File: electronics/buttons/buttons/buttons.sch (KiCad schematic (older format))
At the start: 12 parts, among them J1 Conn_01x02_Male, J2 Conn_01x03_Male, J3 Conn_01x03_Male

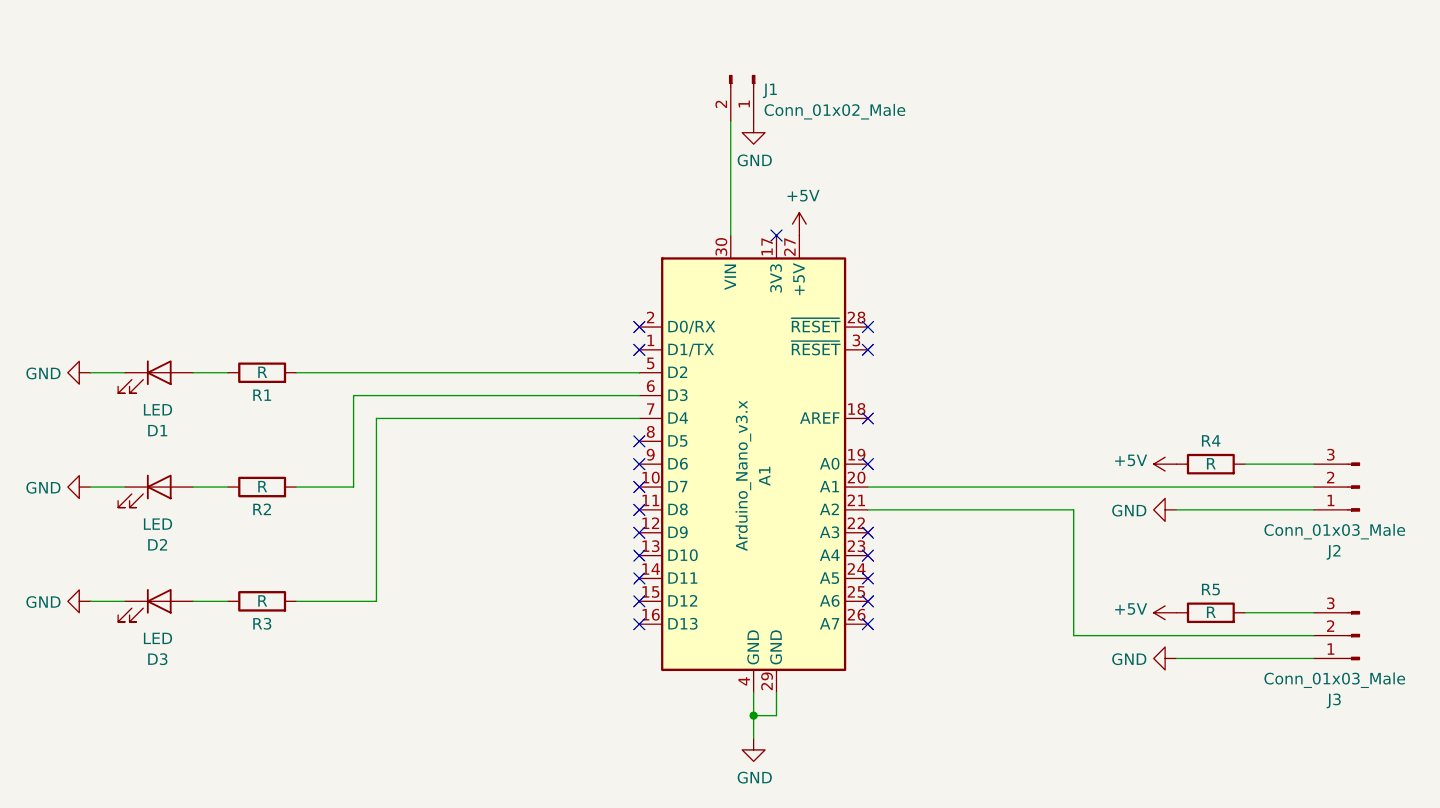
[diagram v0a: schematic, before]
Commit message: change button pcb layout. Added fab files
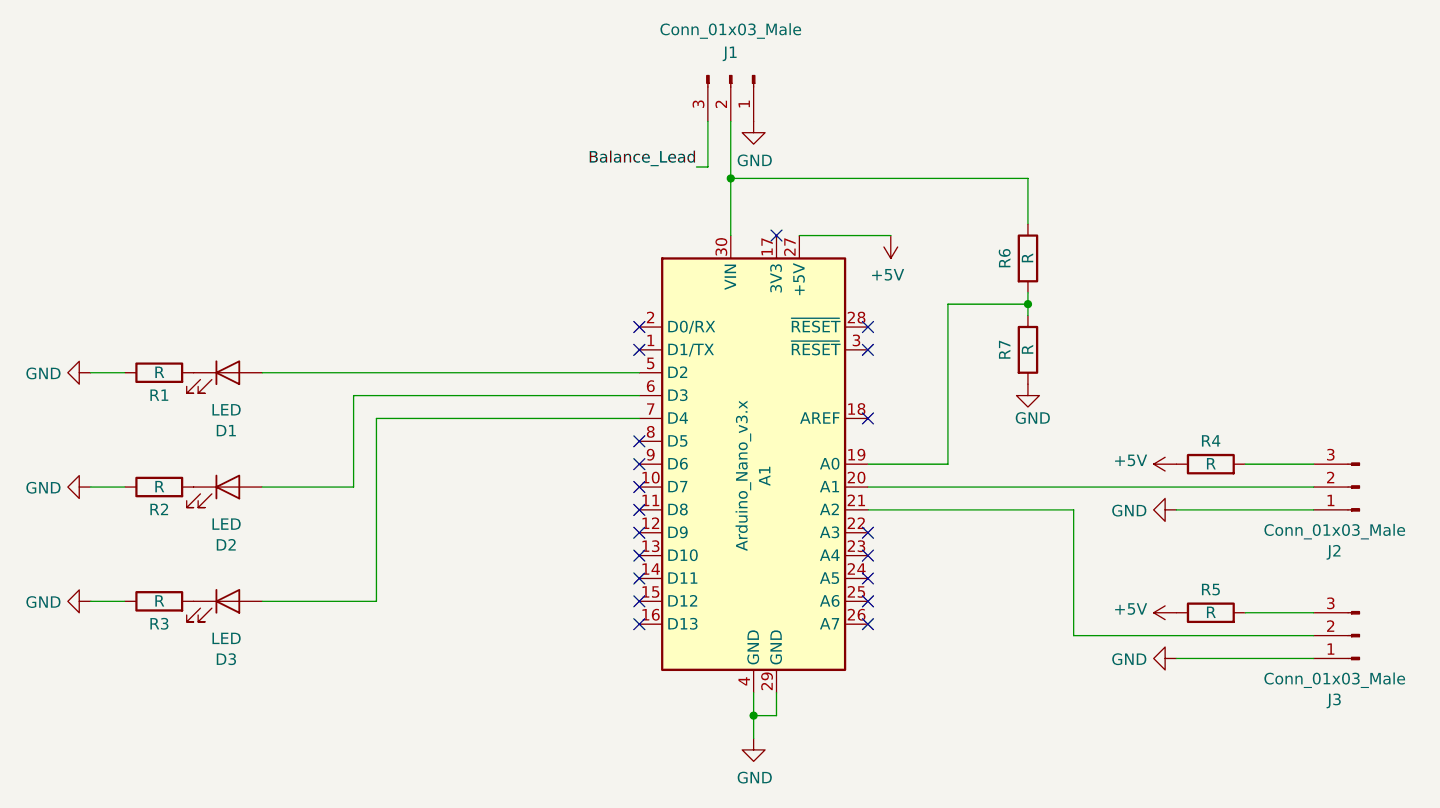
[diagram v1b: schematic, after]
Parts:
- removed J1: Conn_01x02_Male, Connector_JST:JST_EH_S2B-EH_1x02_P2.50mm_Horizontal, symbol Connector:Conn_01x02_Male
- added J1: Conn_01x03_Male, Connector_PinHeader_2.54mm:PinHeader_1x03_P2.54mm_Vertical, symbol Connector:Conn_01x03_Male
- added R6, R7: R, Resistor_SMD:R_1206_3216Metric_Pad1.42x1.75mm_HandSolder, symbol Device:R
- A1: footprint Module:Arduino_Nano -> 1_Project_Specific:NANO_33_Footprint_SMD_Castell
- J2, J3: footprint Connector_JST:JST_XH_B3B-XH-A_1x03_P2.50mm_Vertical -> Connector_PinHeader_2.54mm:PinHeader_1x03_P2.54mm_Vertical
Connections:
- net GND: now also R1.1, R2.1, R3.1, J1.1 (Pin_1), R7.2; no longer D1.1 (K), D2.1 (K), D3.1 (K)
- net at A1.19 (A0): now also R6.2, R7.1
- net at A1.30 (VIN): now also J1.2 (Pin_2), R6.1
- net at A1.5 (D2): now also D1.2 (A); no longer R1.2
- net at A1.6 (D3): now also D2.2 (A); no longer R2.2
- net at A1.7 (D4): now also D3.2 (A); no longer R3.2
- new net: D3.1 (K), R3.2
- new net: D2.1 (K), R2.2
- new net: D1.1 (K), R1.2
- new net Balance_Lead: J1.3 (Pin_3)
- no-connect marks 21 -> 20
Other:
- moved on the sheet: D1, D2, D3, R1, R2, R3
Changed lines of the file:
@@
 F 0 "A1" V 4800 3300 50  0000 C CNN
 F 1 "Arduino_Nano_v3.x" V 4700 3300 50  0000 C CNN
-F 2 "Module:Arduino_Nano" H 4750 3350 50  0001 C CIN
+F 2 "1_Project_Specific:NANO_33_Footprint_SMD_Castell" H 4750 3350 50  0001 C CIN
 F 3 "http://www.mouser.com/pdfdocs/Gravitech_Arduino_Nano3_0.pdf" H 4750 3350 50  0001 C CNN
 	1    4750 3350
@@
 L Device:LED D3
 U 1 1 5E72B9A4
+P 2450 3950
+F 0 "D3" H 2443 3695 50  0000 C CNN
+F 1 "LED" H 2443 3786 50  0000 C CNN
+F 2 "LED_THT:LED_D5.0mm" H 2450 3950 50  0001 C CNN
+F 3 "~" H 2450 3950 50  0001 C CNN
+	1    2450 3950
+	1    0    0    -1
+$EndComp
+$Comp
+L Device:LED D2
+U 1 1 5E72CADD
+P 2450 3450
+F 0 "D2" H 2443 3195 50  0000 C CNN
+F 1 "LED" H 2443 3286 50  0000 C CNN
+F 2 "LED_THT:LED_D5.0mm" H 2450 3450 50  0001 C CNN
+F 3 "~" H 2450 3450 50  0001 C CNN
+	1    2450 3450
+	1    0    0    -1
+$EndComp
+$Comp
+L Device:LED D1
+U 1 1 5E72CFE8
+P 2450 2950
+F 0 "D1" H 2443 2695 50  0000 C CNN
+F 1 "LED" H 2443 2786 50  0000 C CNN
+F 2 "LED_THT:LED_D5.0mm" H 2450 2950 50  0001 C CNN
+F 3 "~" H 2450 2950 50  0001 C CNN
+	1    2450 2950
+	1    0    0    -1
+$EndComp
+$Comp
+L Device:R R3
+U 1 1 5E72D9E9
 P 2150 3950
-F 0 "D3" H 2143 3695 50  0000 C CNN
-F 1 "LED" H 2143 3786 50  0000 C CNN
-F 2 "LED_THT:LED_D5.0mm" H 2150 3950 50  0001 C CNN
+F 0 "R3" V 2050 3950 50  0000 C CNN
+F 1 "R" V 2150 3950 50  0000 C CNN
+F 2 "Resistor_SMD:R_1206_3216Metric_Pad1.42x1.75mm_HandSolder" V 2080 3950 50  0001 C CNN
 F 3 "~" H 2150 3950 50  0001 C CNN
 	1    2150 3950
-	1    0    0    -1
-$EndComp
-$Comp
-L Device:LED D2
-U 1 1 5E72CADD
+	0    -1   -1   0
+$EndComp
+$Comp
+L Device:R R2
+U 1 1 5E72E3E8
 P 2150 3450
-F 0 "D2" H 2143 3195 50  0000 C CNN
-F 1 "LED" H 2143 3286 50  0000 C CNN
-F 2 "LED_THT:LED_D5.0mm" H 2150 3450 50  0001 C CNN
+F 0 "R2" V 2050 3450 50  0000 C CNN
+F 1 "R" V 2150 3450 50  0000 C CNN
+F 2 "Resistor_SMD:R_1206_3216Metric_Pad1.42x1.75mm_HandSolder" V 2080 3450 50  0001 C CNN
 F 3 "~" H 2150 3450 50  0001 C CNN
 	1    2150 3450
-	1    0    0    -1
-$EndComp
-$Comp
-L Device:LED D1
-U 1 1 5E72CFE8
+	0    -1   -1   0
+$EndComp
+$Comp
+L Device:R R1
+U 1 1 5E72E9E3
 P 2150 2950
-F 0 "D1" H 2143 2695 50  0000 C CNN
-F 1 "LED" H 2143 2786 50  0000 C CNN
-F 2 "LED_THT:LED_D5.0mm" H 2150 2950 50  0001 C CNN
+F 0 "R1" V 2050 2950 50  0000 C CNN
+F 1 "R" V 2150 2950 50  0000 C CNN
+F 2 "Resistor_SMD:R_1206_3216Metric_Pad1.42x1.75mm_HandSolder" V 2080 2950 50  0001 C CNN
 F 3 "~" H 2150 2950 50  0001 C CNN
 	1    2150 2950
-	1    0    0    -1
-$EndComp
-$Comp
-L Device:R R3
-U 1 1 5E72D9E9
-P 2600 3950
-F 0 "R3" V 2500 3950 50  0000 C CNN
-F 1 "R" V 2600 3950 50  0000 C CNN
-F 2 "Resistor_SMD:R_1206_3216Metric_Pad1.42x1.75mm_HandSolder" V 2530 3950 50  0001 C CNN
-F 3 "~" H 2600 3950 50  0001 C CNN
-	1    2600 3950
-	0    -1   -1   0
-$EndComp
-$Comp
-L Device:R R2
-U 1 1 5E72E3E8
-P 2600 3450
-F 0 "R2" V 2500 3450 50  0000 C CNN
-F 1 "R" V 2600 3450 50  0000 C CNN
-F 2 "Resistor_SMD:R_1206_3216Metric_Pad1.42x1.75mm_HandSolder" V 2530 3450 50  0001 C CNN
-F 3 "~" H 2600 3450 50  0001 C CNN
-	1    2600 3450
-	0    -1   -1   0
-$EndComp
-$Comp
-L Device:R R1
-U 1 1 5E72E9E3
-P 2600 2950
-F 0 "R1" V 2500 2950 50  0000 C CNN
-F 1 "R" V 2600 2950 50  0000 C CNN
-F 2 "Resistor_SMD:R_1206_3216Metric_Pad1.42x1.75mm_HandSolder" V 2530 2950 50  0001 C CNN
-F 3 "~" H 2600 2950 50  0001 C CNN
-	1    2600 2950
 	0    -1   -1   0
 $EndComp
@@
 F 0 "J2" H 7508 3731 50  0000 C CNN
 F 1 "Conn_01x03_Male" H 7508 3640 50  0000 C CNN
-F 2 "Connector_JST:JST_XH_B3B-XH-A_1x03_P2.50mm_Vertical" H 7400 3450 50  0001 C CNN
+F 2 "Connector_PinHeader_2.54mm:PinHeader_1x03_P2.54mm_Vertical" H 7400 3450 50  0001 C CNN
 F 3 "~" H 7400 3450 50  0001 C CNN
 	1    7400 3450
@@
 F 0 "J3" H 7508 4381 50  0000 C CNN
 F 1 "Conn_01x03_Male" H 7508 4290 50  0000 C CNN
-F 2 "Connector_JST:JST_XH_B3B-XH-A_1x03_P2.50mm_Vertical" H 7400 4100 50  0001 C CNN
+F 2 "Connector_PinHeader_2.54mm:PinHeader_1x03_P2.54mm_Vertical" H 7400 4100 50  0001 C CNN
 F 3 "~" H 7400 4100 50  0001 C CNN
 	1    7400 4100
 	-1   0    0    1
 $EndComp
-Wire Wire Line
-	2450 3450 2300 3450
-Wire Wire Line
-	2450 3950 2300 3950
-Wire Wire Line
-	2450 2950 2300 2950
 Wire Wire Line
 	6900 3350 7200 3350
@@
 	3000 3050 3000 3450
 Wire Wire Line
-	3000 3450 2750 3450
-Wire Wire Line
 	3100 3150 3100 3950
-Wire Wire Line
-	3100 3950 2750 3950
-Wire Wire Line
-	2750 2950 4250 2950
 Wire Wire Line
 	3000 3050 4250 3050
@@
 	1    0    0    -1
 $EndComp
-$Comp
-L Connector:Conn_01x02_Male J1
-U 1 1 5E762A53
-P 4750 1650
-F 0 "J1" V 4812 1694 50  0000 L CNN
-F 1 "Conn_01x02_Male" V 4903 1694 50  0000 L CNN
-F 2 "Connector_JST:JST_EH_S2B-EH_1x02_P2.50mm_Horizontal" H 4750 1650 50  0001 C CNN
-F 3 "~" H 4750 1650 50  0001 C CNN
-	1    4750 1650
-	0    1    1    0
-$EndComp
-Wire Wire Line
-	4650 2350 4650 1850
-$Comp
-L power:GND #PWR0109
-U 1 1 5E764900
-P 4750 1850
-F 0 "#PWR0109" H 4750 1600 50  0001 C CNN
-F 1 "GND" H 4755 1677 50  0000 C CNN
-F 2 "" H 4750 1850 50  0001 C CNN
-F 3 "" H 4750 1850 50  0001 C CNN
-	1    4750 1850
-	1    0    0    -1
-$EndComp
+Wire Wire Line
+	4650 2350 4650 2100
 $Comp
 L power:+5V #PWR0110
 U 1 1 5E7657A9
-P 4950 2350
-F 0 "#PWR0110" H 4950 2200 50  0001 C CNN
-F 1 "+5V" H 4965 2523 50  0000 C CNN
-F 2 "" H 4950 2350 50  0001 C CNN
-F 3 "" H 4950 2350 50  0001 C CNN
-	1    4950 2350
-	1    0    0    -1
+P 5350 2350
+F 0 "#PWR0110" H 5350 2200 50  0001 C CNN
+F 1 "+5V" H 5365 2523 50  0000 C CNN
+F 2 "" H 5350 2350 50  0001 C CNN
+F 3 "" H 5350 2350 50  0001 C CNN
+	1    5350 2350
+	-1   0    0    1
 $EndComp
 NoConn ~ 4850 2350
@@
 NoConn ~ 5250 3750
 NoConn ~ 5250 3650
-NoConn ~ 5250 3350
+$Comp
+L Connector:Conn_01x03_Male J1
+U 1 1 5E737BF0
+P 4650 1650
+F 0 "J1" V 4550 1650 50  0000 C CNN
+F 1 "Conn_01x03_Male" V 4450 1650 50  0000 C CNN
+F 2 "Connector_PinHeader_2.54mm:PinHeader_1x03_P2.54mm_Vertical" H 4650 1650 50  0001 C CNN
+F 3 "~" H 4650 1650 50  0001 C CNN
+	1    4650 1650
+	0    1    1    0
+$EndComp
+$Comp
+L power:GND #PWR0109
+U 1 1 5E764900
+P 4750 1850
+F 0 "#PWR0109" H 4750 1600 50  0001 C CNN
+F 1 "GND" H 4755 1677 50  0000 C CNN
+F 2 "" H 4750 1850 50  0001 C CNN
+F 3 "" H 4750 1850 50  0001 C CNN
+	1    4750 1850
+	1    0    0    -1
+$EndComp
+$Comp
+L Device:R R7
+U 1 1 5E73B84A
+P 5950 2850
+F 0 "R7" V 5850 2850 50  0000 C CNN
+F 1 "R" V 5950 2850 50  0000 C CNN
+F 2 "Resistor_SMD:R_1206_3216Metric_Pad1.42x1.75mm_HandSolder" V 5880 2850 50  0001 C CNN
+F 3 "~" H 5950 2850 50  0001 C CNN
+	1    5950 2850
+	1    0    0    -1
+$EndComp
+$Comp
+L Device:R R6
+U 1 1 5E73D40E
+P 5950 2450
+F 0 "R6" V 5850 2450 50  0000 C CNN
+F 1 "R" V 5950 2450 50  0000 C CNN
+F 2 "Resistor_SMD:R_1206_3216Metric_Pad1.42x1.75mm_HandSolder" V 5880 2450 50  0001 C CNN
+F 3 "~" H 5950 2450 50  0001 C CNN
+	1    5950 2450
+	1    0    0    -1
+$EndComp
+Wire Wire Line
+	4650 2100 5950 2100
+Connection ~ 4650 2100
+Wire Wire Line
+	4650 2100 4650 1850
+Wire Wire Line
+	4950 2350 5350 2350
+Wire Wire Line
+	5950 2600 5950 2650
+$Comp
+L power:GND #PWR01
+U 1 1 5E745127
+P 5950 3000
+F 0 "#PWR01" H 5950 2750 50  0001 C CNN
+F 1 "GND" H 6050 2850 50  0000 R CNN
+F 2 "" H 5950 3000 50  0001 C CNN
+F 3 "" H 5950 3000 50  0001 C CNN
+	1    5950 3000
+	1    0    0    -1
+$EndComp
+Wire Wire Line
+	5950 2100 5950 2300
+Wire Wire Line
+	5950 2650 5600 2650
+Wire Wire Line
+	5600 2650 5600 3350
+Wire Wire Line
+	5600 3350 5250 3350
+Connection ~ 5950 2650
+Wire Wire Line
+	5950 2650 5950 2700
+Text Label 4500 2050 2    50   ~ 0
+Balance_Lead
+Wire Wire Line
+	4550 1850 4550 2050
+Wire Wire Line
+	4550 2050 4500 2050
+Wire Wire Line
+	2600 3450 3000 3450
+Wire Wire Line
+	2600 3950 3100 3950
+Wire Wire Line
+	2600 2950 4250 2950
 $EndSCHEMATC

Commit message: v2 arduino code
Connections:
- net Balance_Lead: now also J1.2 (Pin_2); no longer J1.3 (Pin_3)
- net at A1.30 (VIN), R6.1: now also J1.3 (Pin_3); no longer J1.2 (Pin_2)
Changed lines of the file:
@@
 Wire Wire Line
 	4650 2100 5950 2100
-Connection ~ 4650 2100
-Wire Wire Line
-	4650 2100 4650 1850
 Wire Wire Line
 	4950 2350 5350 2350
@@
 Wire Wire Line
 	5950 2650 5950 2700
-Text Label 4500 2050 2    50   ~ 0
-Balance_Lead
-Wire Wire Line
-	4550 1850 4550 2050
-Wire Wire Line
-	4550 2050 4500 2050
 Wire Wire Line
 	2600 3450 3000 3450
@@
 Wire Wire Line
 	2600 2950 4250 2950
+Text Label 3950 2050 0    50   ~ 0
+Balance_Lead
+Wire Wire Line
+	4550 2100 4650 2100
+Connection ~ 4650 2100
+Wire Wire Line
+	4650 1850 4650 2050
+Wire Wire Line
+	4550 1850 4550 2100
+Wire Wire Line
+	3950 2050 4650 2050
 $EndSCHEMATC
